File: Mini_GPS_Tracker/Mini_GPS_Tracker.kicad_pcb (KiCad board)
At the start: 4 copper layers, 38.1 x 99.1 mm, 56 parts, among them J1 USB_C_Receptacle, J2 Screw_Terminal_01x02, J3 901-10512-1, J4 Conn_ARM_JTAG_SWD_10, SW1 SW_Push, SW2 MLL1200S, U1 CH340E, U2 MS5611-01BA, U3 LD1117S33TR_SOT223, U4 MAX-8Q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

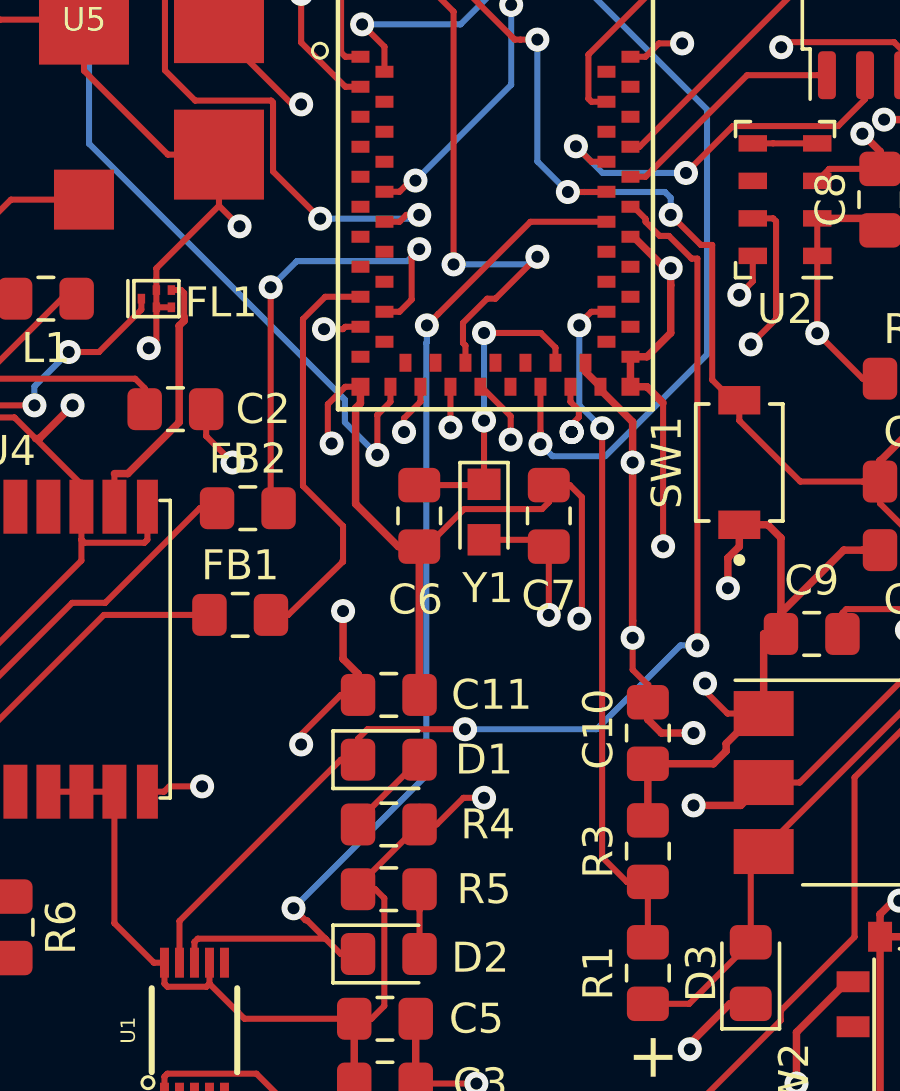
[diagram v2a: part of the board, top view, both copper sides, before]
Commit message: fixed tx route
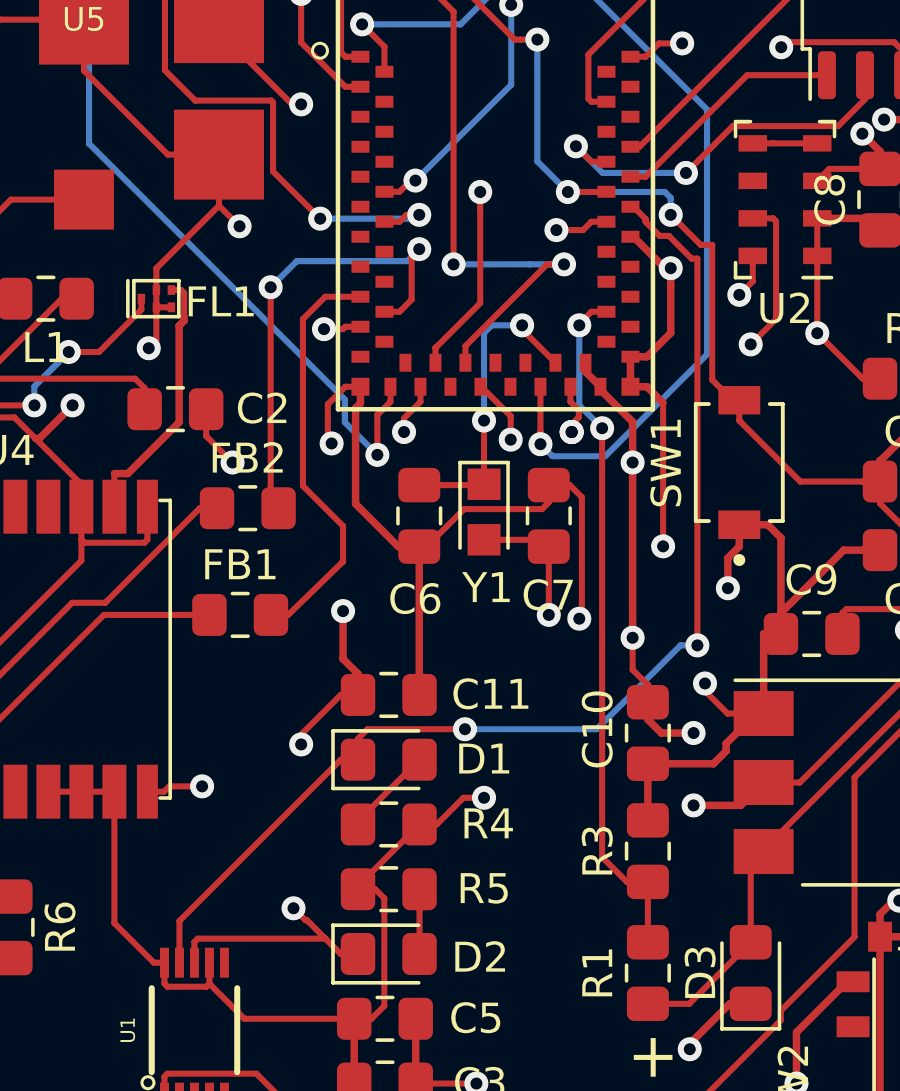
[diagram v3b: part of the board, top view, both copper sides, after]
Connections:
- MD1 pad 26: Net-(MD1-Pad26) -> TRANS_RX
- MD1 pad 27: TRANS_RX -> Net-(MD1-Pad27)
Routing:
- net TRANS_RX: track 49.6 -> 47.4 mm
- net TRANS_TX: track 52.7 -> 53.7 mm
- net RXI: track 36.6 -> 35.9 mm
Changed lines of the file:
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@@
     (thickness 1.6)
     (drawings 5)
-    (tracks 1000)
+    (tracks 1004)
     (zones 0)
     (modules 56)
@@
   (net 27 "Net-(MD1-Pad32)")
   (net 28 "Net-(MD1-Pad30)")
-  (net 29 "Net-(MD1-Pad26)")
-  (net 30 "Net-(MD1-Pad24)")
-  (net 31 "Net-(MD1-Pad31)")
+  (net 29 "Net-(MD1-Pad24)")
+  (net 30 "Net-(MD1-Pad31)")
+  (net 31 "Net-(MD1-Pad27)")
   (net 32 "Net-(MD1-Pad57)")
   (net 33 "Net-(MD1-Pad55)")
@@
     (add_net "Net-(MD1-Pad21)")
     (add_net "Net-(MD1-Pad24)")
-    (add_net "Net-(MD1-Pad26)")
+    (add_net "Net-(MD1-Pad27)")
     (add_net "Net-(MD1-Pad30)")
     (add_net "Net-(MD1-Pad31)")
@@
       (net 45 TRANS_TX))
     (pad 26 smd rect (at -2 6.2) (size 0.4 0.6) (layers F.Cu F.Paste F.Mask)
-      (net 29 "Net-(MD1-Pad26)"))
+      (net 43 TRANS_RX))
     (pad 24 smd rect (at -3 6.2) (size 0.4 0.6) (layers F.Cu F.Paste F.Mask)
-      (net 30 "Net-(MD1-Pad24)"))
+      (net 29 "Net-(MD1-Pad24)"))
     (pad 37 smd rect (at 3.5 7) (size 0.4 0.6) (layers F.Cu F.Paste F.Mask)
       (net 3 +3V3))
@@
       (net 104 A1))
     (pad 31 smd rect (at 0.5 7) (size 0.4 0.6) (layers F.Cu F.Paste F.Mask)
-      (net 31 "Net-(MD1-Pad31)"))
+      (net 30 "Net-(MD1-Pad31)"))
     (pad 29 smd rect (at -0.5 7) (size 0.4 0.6) (layers F.Cu F.Paste F.Mask)
       (net 115 gps_reset))
     (pad 27 smd rect (at -1.5 7) (size 0.4 0.6) (layers F.Cu F.Paste F.Mask)
-      (net 43 TRANS_RX))
+      (net 31 "Net-(MD1-Pad27)"))
     (pad 25 smd rect (at -2.5 7) (size 0.4 0.6) (layers F.Cu F.Paste F.Mask)
       (net 53 Pressure_SDA))
@@
   (segment (start 168.529 104.775) (end 168.529 104.775) (width 0.203) (layer F.Cu) (net 4))
   (via (at 168.529 104.775) (size 0.8) (drill 0.4) (layers F.Cu B.Cu) (net 4))
-  (segment (start 170.91 102.344) (end 170.42 101.854) (width 0.203) (layer F.Cu) (net 4))
-  (segment (start 170.91 102.847) (end 170.91 102.344) (width 0.203) (layer F.Cu) (net 4))
-  (segment (start 170.42 101.854) (end 168.529 101.854) (width 0.203) (layer F.Cu) (net 4))
-  (segment (start 168.529 101.854) (end 168.529 101.854) (width 0.203) (layer F.Cu) (net 4))
-  (via (at 168.529 101.854) (size 0.8) (drill 0.4) (layers F.Cu B.Cu) (net 4))
+  (via (at 169.799 101.6) (size 0.8) (drill 0.4) (layers F.Cu B.Cu) (net 4))
   (segment (start 168.529 104.775) (end 168.529 101.854) (width 0.203) (layer B.Cu) (net 4))
+  (segment (start 168.783 101.6) (end 169.799 101.6) (width 0.203) (layer B.Cu) (net 4))
+  (segment (start 168.529 101.854) (end 168.783 101.6) (width 0.203) (layer B.Cu) (net 4))
+  (segment (start 169.799 101.736) (end 170.91 102.847) (width 0.203) (layer F.Cu) (net 4))
+  (segment (start 169.799 101.6) (end 169.799 101.736) (width 0.203) (layer F.Cu) (net 4))
   (segment (start 170.461 108.748) (end 170.688 108.975) (width 0.203) (layer F.Cu) (net 5))
   (segment (start 168.529 108.748) (end 170.461 108.748) (width 0.203) (layer F.Cu) (net 5))
@@
   (segment (start 163.754 122.555) (end 164.329 122.555) (width 0.203) (layer F.Cu) (net 8))
   (segment (start 158.877 122.845) (end 158.877 122.152298) (width 0.203) (layer F.Cu) (net 8))
-  (via (at 166.624 101.6) (size 0.8) (drill 0.4) (layers F.Cu B.Cu) (net 8))
   (segment (start 162.179 121.031) (end 162.179 121.031) (width 0.203) (layer B.Cu) (net 8))
   (via (at 162.179 121.031) (size 0.8) (drill 0.4) (layers F.Cu B.Cu) (net 8))
@@
   (segment (start 162.578999 121.430999) (end 162.629999 121.430999) (width 0.203) (layer F.Cu) (net 8))
   (segment (start 162.179 121.031) (end 162.578999 121.430999) (width 0.203) (layer F.Cu) (net 8))
-  (segment (start 162.179 121.031) (end 166.605001 116.604999) (width 0.203) (layer B.Cu) (net 8))
-  (segment (start 167.005 101.219) (end 166.624 101.6) (width 0.203) (layer F.Cu) (net 8))
-  (segment (start 170.077 98.147) (end 167.005 101.219) (width 0.203) (layer F.Cu) (net 8))
-  (segment (start 172.61 98.147) (end 170.077 98.147) (width 0.203) (layer F.Cu) (net 8))
-  (segment (start 166.605001 102.184684) (end 166.605001 116.604999) (width 0.203) (layer B.Cu) (net 8))
-  (segment (start 166.624 102.165685) (end 166.605001 102.184684) (width 0.203) (layer B.Cu) (net 8))
-  (segment (start 166.624 101.6) (end 166.624 102.165685) (width 0.203) (layer B.Cu) (net 8))
+  (segment (start 172.107 98.147) (end 171.829 98.425) (width 0.203) (layer F.Cu) (net 8))
+  (segment (start 172.61 98.147) (end 172.107 98.147) (width 0.203) (layer F.Cu) (net 8))
+  (segment (start 171.829 98.425) (end 170.942 98.425) (width 0.203) (layer F.Cu) (net 8))
+  (segment (start 170.942 98.425) (end 170.942 98.425) (width 0.203) (layer F.Cu) (net 8))
+  (via (at 170.942 98.425) (size 0.8) (drill 0.4) (layers F.Cu B.Cu) (net 8))
+  (segment (start 170.542001 98.824999) (end 170.942 98.425) (width 0.203) (layer PWR) (net 8))
+  (segment (start 167.827499 114.090279) (end 167.827499 101.539501) (width 0.203) (layer PWR) (net 8))
+  (segment (start 167.827499 101.539501) (end 170.542001 98.824999) (width 0.203) (layer PWR) (net 8))
+  (segment (start 162.179 119.738778) (end 167.827499 114.090279) (width 0.203) (layer PWR) (net 8))
+  (segment (start 162.179 121.031) (end 162.179 119.738778) (width 0.203) (layer PWR) (net 8))
   (segment (start 166.379 121.096) (end 166.379 122.555) (width 0.203) (layer F.Cu) (net 9))
   (segment (start 166.379 120.396) (end 166.379 121.096) (width 0.203) (layer F.Cu) (net 9))
@@
   (segment (start 159.430998 62.394) (end 158.450999 63.373999) (width 0.25) (layer F.Cu) (net 43))
   (segment (start 160.196 62.394) (end 159.430998 62.394) (width 0.25) (layer F.Cu) (net 43))
-  (segment (start 167.41 103.647) (end 167.41 105.005) (width 0.203) (layer F.Cu) (net 43))
-  (segment (start 167.41 105.005) (end 167.41 105.005) (width 0.203) (layer F.Cu) (net 43))
-  (via (at 167.41 105.005) (size 0.8) (drill 0.4) (layers F.Cu B.Cu) (net 43))
   (segment (start 158.450999 63.373999) (end 158.450999 81.414001) (width 0.25) (layer F.Cu) (net 43))
   (segment (start 158.493299 81.414001) (end 160.391298 83.312) (width 0.203) (layer F.Cu) (net 43))
@@
   (segment (start 163.134501 84.902501) (end 161.544 83.312) (width 0.203) (layer PWR) (net 43))
   (segment (start 164.128279 92.268501) (end 163.134501 91.274723) (width 0.203) (layer PWR) (net 43))
-  (segment (start 164.128279 101.723279) (end 164.128279 92.268501) (width 0.203) (layer PWR) (net 43))
-  (segment (start 167.41 105.005) (end 164.128279 101.723279) (width 0.203) (layer PWR) (net 43))
+  (segment (start 166.91 102.847) (end 166.91 102.344) (width 0.203) (layer F.Cu) (net 43))
+  (via (at 168.402 97.155) (size 0.8) (drill 0.4) (layers F.Cu B.Cu) (net 43))
+  (segment (start 164.128279 92.268501) (end 164.658501 92.268501) (width 0.203) (layer PWR) (net 43))
+  (segment (start 164.658501 93.411501) (end 168.402 97.155) (width 0.203) (layer PWR) (net 43))
+  (segment (start 164.658501 92.268501) (end 164.658501 93.411501) (width 0.203) (layer PWR) (net 43))
+  (segment (start 168.402 100.860222) (end 168.402 97.720685) (width 0.203) (layer F.Cu) (net 43))
+  (segment (start 166.918222 102.344) (end 168.402 100.860222) (width 0.203) (layer F.Cu) (net 43))
+  (segment (start 168.402 97.720685) (end 168.402 97.155) (width 0.203) (layer F.Cu) (net 43))
+  (segment (start 166.91 102.344) (end 166.918222 102.344) (width 0.203) (layer F.Cu) (net 43))
   (segment (start 158.00099 81.630988) (end 165.835001 89.464999) (width 0.25) (layer F.Cu) (net 45))
   (segment (start 158.00099 60.91901) (end 158.00099 81.630988) (width 0.25) (layer F.Cu) (net 45))
@@
   (segment (start 167.513 99.568) (end 167.513 99.568) (width 0.203) (layer F.Cu) (net 45))
   (via (at 167.513 99.568) (size 0.8) (drill 0.4) (layers F.Cu B.Cu) (net 45))
-  (segment (start 167.827499 101.517279) (end 168.633778 100.711) (width 0.203) (layer F.Cu) (net 45))
-  (segment (start 167.827499 102.190721) (end 167.827499 101.517279) (width 0.203) (layer F.Cu) (net 45))
-  (segment (start 167.91 102.273222) (end 167.827499 102.190721) (width 0.203) (layer F.Cu) (net 45))
-  (segment (start 167.91 102.847) (end 167.91 102.273222) (width 0.203) (layer F.Cu) (net 45))
-  (via (at 170.307 99.314) (size 0.8) (drill 0.4) (layers F.Cu B.Cu) (net 45))
-  (segment (start 168.91 100.711) (end 170.307 99.314) (width 0.203) (layer F.Cu) (net 45))
-  (segment (start 168.633778 100.711) (end 168.91 100.711) (width 0.203) (layer F.Cu) (net 45))
-  (segment (start 170.053 99.568) (end 170.307 99.314) (width 0.203) (layer B.Cu) (net 45))
   (segment (start 167.513 99.568) (end 170.053 99.568) (width 0.203) (layer B.Cu) (net 45))
+  (segment (start 170.053 99.568) (end 171.196 99.568) (width 0.203) (layer B.Cu) (net 45))
+  (segment (start 171.196 99.568) (end 171.196 99.568) (width 0.203) (layer B.Cu) (net 45))
+  (via (at 171.196 99.568) (size 0.8) (drill 0.4) (layers F.Cu B.Cu) (net 45))
+  (segment (start 170.630315 99.568) (end 171.196 99.568) (width 0.203) (layer F.Cu) (net 45))
+  (segment (start 167.91 102.288315) (end 170.630315 99.568) (width 0.203) (layer F.Cu) (net 45))
+  (segment (start 167.91 102.847) (end 167.91 102.288315) (width 0.203) (layer F.Cu) (net 45))
   (segment (start 174.989457 128.199499) (end 165.170501 128.199499) (width 0.203) (layer F.Cu) (net 51))
   (segment (start 178.42051 124.768446) (end 174.989457 128.199499) (width 0.203) (layer F.Cu) (net 51))
@@
   (via (at 163.195 101.727) (size 0.8) (drill 0.4) (layers F.Cu B.Cu) (net 52))
   (segment (start 164.338 100.584) (end 163.195 101.727) (width 0.203) (layer GND) (net 52))
-  (segment (start 177.038 100.584) (end 164.338 100.584) (width 0.203) (layer GND) (net 52))
+  (segment (start 164.338 100.584) (end 177.038 100.584) (width 0.203) (layer GND) (net 52))
   (segment (start 166.41 104.15) (end 165.862 104.698) (width 0.203) (layer F.Cu) (net 53))
   (segment (start 166.41 103.647) (end 166.41 104.15) (width 0.203) (layer F.Cu) (net 53))

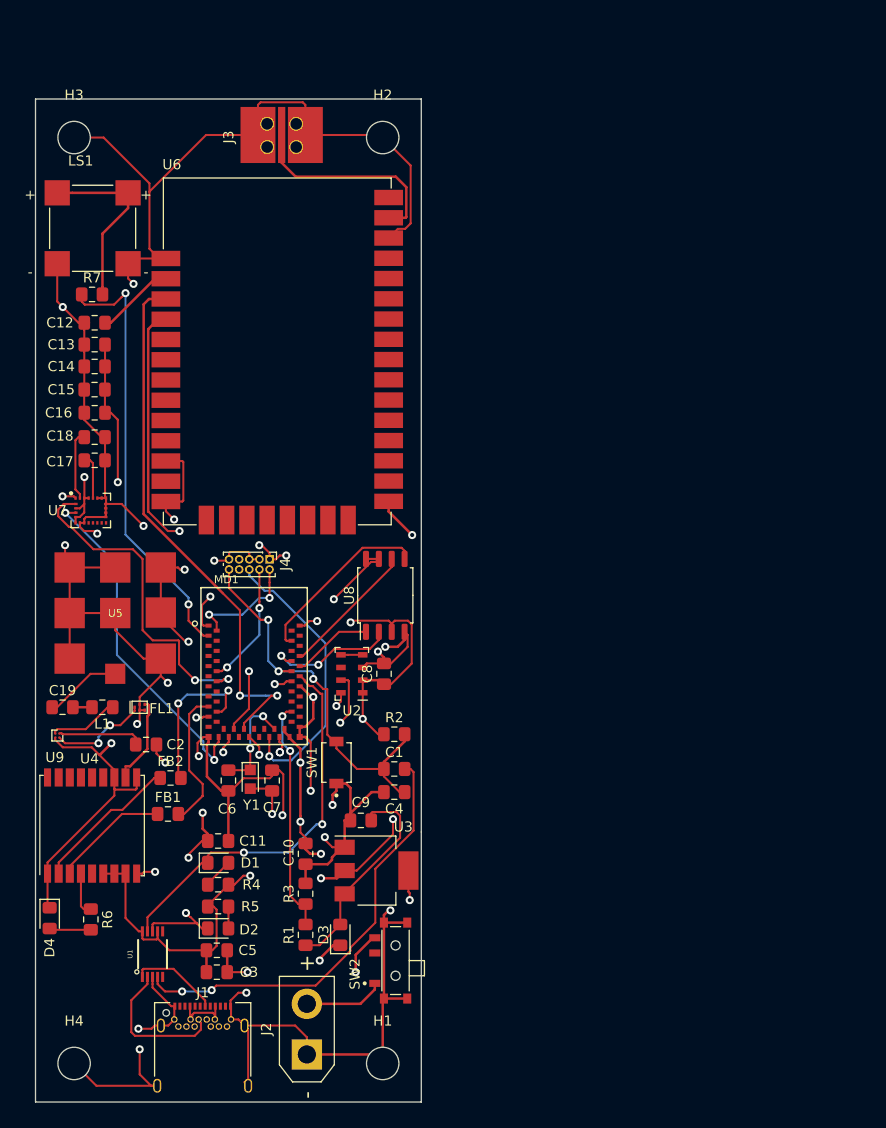
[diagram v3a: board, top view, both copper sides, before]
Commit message: added power and power pours
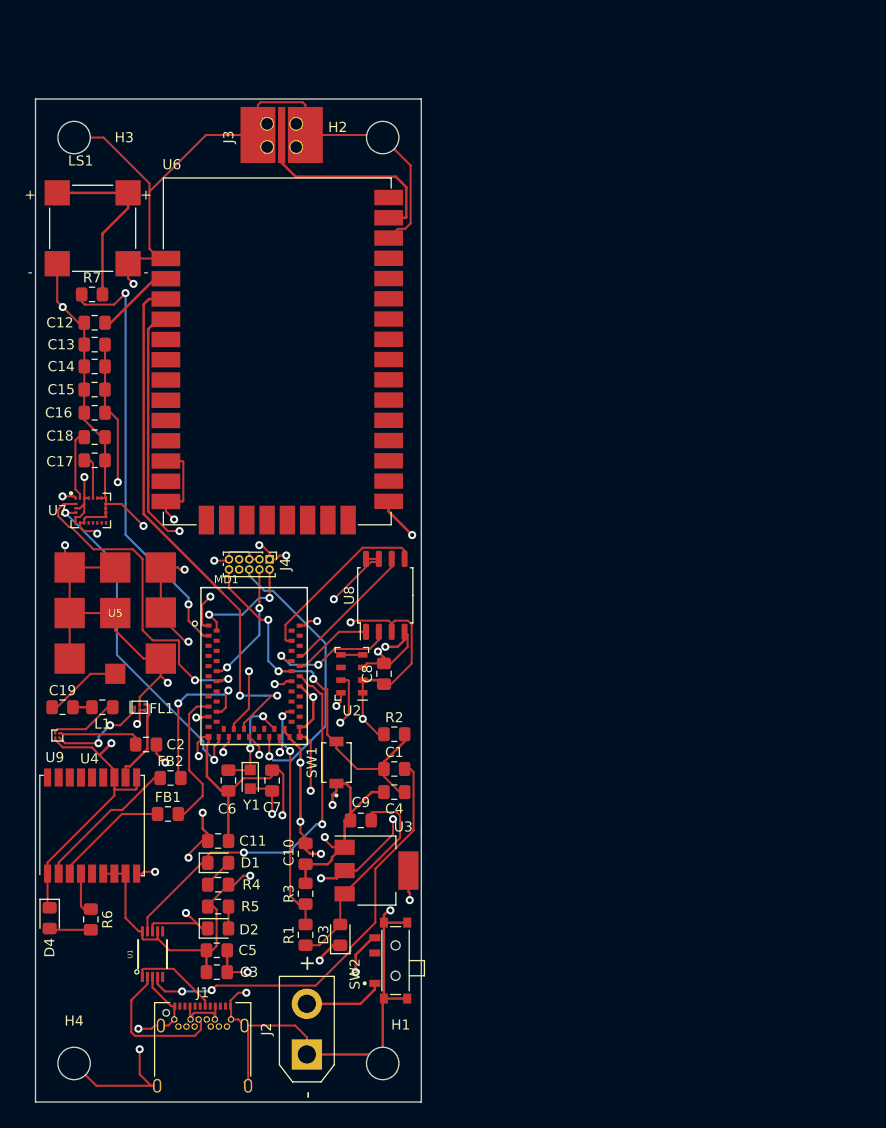
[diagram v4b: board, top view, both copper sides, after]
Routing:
- added copper zone on GND, net GND
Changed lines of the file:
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@@
     (tags "mounting hole 3.2mm no annular m3")
     (attr virtual)
-    (fp_text reference H1 (at 0 -4.2) (layer F.SilkS)
+    (fp_text reference H1 (at 1.778 -3.81) (layer F.SilkS)
       (effects (font (size 1 1) (thickness 0.15)))
     )
@@
     (tags "mounting hole 3.2mm no annular m3")
     (attr virtual)
-    (fp_text reference H2 (at 0 -4.2) (layer F.SilkS)
+    (fp_text reference H2 (at -4.445 -1.016) (layer F.SilkS)
       (effects (font (size 1 1) (thickness 0.15)))
     )
@@
     (tags "mounting hole 3.2mm no annular m3")
     (attr virtual)
-    (fp_text reference H3 (at 0 -4.2) (layer F.SilkS)
+    (fp_text reference H3 (at 4.953 0) (layer F.SilkS)
       (effects (font (size 1 1) (thickness 0.15)))
     )
@@
       )
     )
+  )
+  (zone (net 2) (net_name GND) (layer GND) (hatch edge 0.508)
+    (connect_pads (clearance 0.508))
+    (min_thickness 0.254)
+    (fill yes (arc_segments 32) (thermal_gap 0.508) (thermal_bridge_width 0.508))
+    (polygon
+      (pts
+        (xy 185.42 139.7) (xy 147.32 139.7) (xy 147.32 40.64) (xy 185.42 40.64)
+      )
+    )

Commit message: updates to routing and fix commit
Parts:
- added C20: 100 nf, Capacitor_SMD:C_0805_2012Metric, F.Cu at (149.9, 127.0)
- C19: value CAP -> 100 nf
- C2: value CAP -> 10 pf
- C6, C7: value CAP -> 15 pf
- J4: footprint Connector_PinHeader_1.00mm:PinHeader_2x05_P1.00mm_Vertical -> Connector_PinHeader_2.54mm:PinHeader_2x05_P2.54mm_Vertical
- L1: value INDUCTOR -> 6.8 nH
- R6: value R -> 750
- R7: value R -> 0 ohm
- U1: value CH340E -> FT230XS; footprint Sparkfun-Artemis:MSOP10 -> Package_SO:SSOP-16_3.9x4.9mm_P0.635mm
- Y1: value Crystal -> 32.786 KHz
- moved J4 7.06 mm to (176.5, 82.5)
- moved LS1 6.35 mm to (152.8, 47.1)
- moved H2 6.35 mm to (181.6, 38.1)
- moved H3 6.35 mm to (151.1, 38.1)
- moved J3 6.10 mm to (171.6, 38.1)
- moved U6 5.34 mm to (171.4, 61.0)
- moved U1 2.74 mm to (156.2, 125.7), turned to 0 degrees
- moved R6 1.65 mm to (151.1, 121.7)
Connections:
- D1 pad 1: TX0 -> RXI
- D2 pad 1: RXI -> TX0
- MD1 pad 26: TRANS_RX -> Net-(MD1-Pad26)
- MD1 pad 27: Net-(MD1-Pad27) -> TRANS_RX
- SW2 pad 1: Net-(J2-Pad2) -> Net-(SW2-Pad1)
- SW2 pad 2: Net-(SW2-Pad2) -> Net-(J2-Pad2)
- U1 pad 1: Net-(J1-PadA7) -> TX0
- U1 pad 10: +3V3 -> Net-(C20-Pad1)
- U1 pad 2: Net-(J1-PadB7) -> RTS
- U1 pad 3: GND -> Net-(C20-Pad1)
- U1 pad 4: RTS -> RXI
- U1 pad 5: Net-(U1-Pad5) -> GND
- U1 pad 7: +3V3 -> Net-(U1-Pad7)
- U1 pad 8: RXI -> Net-(J1-PadB7)
- U1 pad 9: TX0 -> Net-(J1-PadA7)
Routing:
- net GND: track 457.5 -> 673.0 mm, vias 28 -> 24
- net Net-(C20-Pad1): track 0.00 -> 22.5 mm, vias 0 -> 2
- net +3V3: track 201.0 -> 214.7 mm, vias 18 -> 19
- net TX0: track 38.8 -> 50.1 mm
- net TRANS_RX: track 47.4 -> 56.0 mm
- net RTS: track 43.0 -> 51.1 mm
- net RXI: track 35.9 -> 43.9 mm, vias 2 -> 3
- net SWDIO: track 11.5 -> 18.8 mm
- net Net-(LS1-PadP1): track 18.1 -> 25.3 mm
- net Net-(C12-Pad1): track 8.43 -> 14.7 mm
- net TRANS_TX: track 53.7 -> 58.4 mm
- net SWDCK: track 12.3 -> 17.0 mm
- net MOSI_Flash: track 18.1 -> 21.8 mm
- net Net-(J1-PadA7): track 8.80 -> 6.54 mm
- net RESET: track 39.5 -> 41.6 mm
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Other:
- board size 38.1 x 99.1 mm -> 38.1 x 105.4 mm

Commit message: updated usb"
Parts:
- added C21: 0.1uF, Capacitor_SMD:C_0805_2012Metric_Pad1.15x1.40mm_HandSolder, F.Cu at (223.4, 119.8)
- added C22: 0.1uF, Capacitor_SMD:C_0805_2012Metric_Pad1.15x1.40mm_HandSolder, F.Cu at (225.4, 125.5)
- added C23: 10uF, Capacitor_SMD:C_0805_2012Metric_Pad1.15x1.40mm_HandSolder, F.Cu at (225.7, 129.9)
- added U10: ADXL343, Package_LGA:LGA-14_3x5mm_P0.8mm_LayoutBorder1x6y, F.Cu at (227.6, 120.8)
- added U11: BNO055, Package_LGA:LGA-28_5.2x3.8mm_P0.5mm, F.Cu at (218.8, 115.4)
- J1: footprint Connector_USB:USB_C_Receptacle_Amphenol_12401548E4-2A -> Connector_USB:USB_C_Receptacle_Amphenol_12401610E4-2A
- moved J1 0.40 mm to (164.0, 135.6)
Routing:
- net GND: track 673.0 -> 672.4 mm
- net Net-(J1-PadB7): track 14.7 -> 15.2 mm, vias 0 -> 2
